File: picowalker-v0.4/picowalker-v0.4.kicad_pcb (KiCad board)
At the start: 4 copper layers, 47.4 x 50.5 mm, 86 parts, among them IC1 RT6150B-33GQW, J1 12402012E212A, J2 BAT, J3 SWD, J4 UART, SW1 ~{BOOT}, SW2 RUN, SW3 BUT_M, SW4 BUT_R, SW5 BUT_L, U1 RP2350A-QFN60, U2 W25Q128JVP, U3 BMA400, U4 M95512DxMC, U5 TFBS4711, U6 BQ25628ERYKR, U7 DO0180FMST0x, Y1 ABM8-272-T3, Y2 SIT1533AI-H4-DCC-32.768E

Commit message: v0.4: good start on routing
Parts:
- removed C15: 0.1u, Capacitor_SMD:C_0402_1005Metric
- added R23: 5.1k, Resistor_SMD:R_0402_1005Metric, F.Cu at (160.1, 108.2)
- added R24: 5.1k, Resistor_SMD:R_0402_1005Metric, F.Cu at (161.6, 108.3)
- added TP6: GP16, picowalker:TestPoint_Pad_D1.0mm_Nosilk, F.Cu at (134.2, 89.7)
- added TP7: GP17, picowalker:TestPoint_Pad_D1.0mm_Nosilk, F.Cu at (131.9, 90.5)
- added U8: DT1240-04LP-7, picowalker:U-DFN2510-10, B.Cu at (148.8, 116.3)
- L2: footprint Inductor_SMD:L_0402_1005Metric -> Inductor_SMD:L_0603_1608Metric
- R2, SW2: moved to B.Cu
- TP1: value MCU_1V1 -> ~{PG}; footprint TestPoint:TestPoint_Pad_1.0x1.0mm -> picowalker:TestPoint_Pad_D1.0mm_Nosilk; moved to F.Cu
- TP2: footprint TestPoint:TestPoint_Pad_1.0x1.0mm -> picowalker:TestPoint_Pad_D1.0mm_Nosilk; moved to F.Cu
- U4: footprint picowalker:XDFN8 -> picowalker:UFDFPN8
- moved R19 29.0 mm to (172.2, 103.4), turned to 180 degrees
- moved TP1 28.2 mm to (173.6, 105.5), turned to 0 degrees
- moved SW2 26.5 mm to (167.1, 85.4), turned to 180 degrees
- moved R2 19.1 mm to (163.1, 84.4), turned to 0 degrees
- moved R9 17.3 mm to (155.4, 113.2), turned to 180 degrees
- moved R12 16.5 mm to (155.4, 112.2)
- moved C17 15.9 mm to (155.4, 111.2)
- moved R15 9.92 mm to (128.9, 102.0), turned to -90 degrees
- moved R7 9.73 mm to (152.6, 115.8), turned to 0 degrees
- moved R10 9.62 mm to (144.1, 113.1), turned to 180 degrees
- moved R13 9.62 mm to (144.1, 112.1)
- moved C18 7.76 mm to (144.1, 111.1)
- moved C22 7.14 mm to (128.9, 100.1), turned to -90 degrees
- moved R20 6.38 mm to (145.0, 106.3)
- moved C20 6.31 mm to (134.1, 95.3), turned to 90 degrees
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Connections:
- net /accel/INT renamed /ACCEL_INT
- net /accel/~{CS} renamed /~{ACCEL_CS}
- net /eeprom/~{CS} renamed /~{EEPROM_CS}
- net /mcu/SOUND_PWM renamed /SOUND
- net /mcu/~{BAT_INT} renamed /~{BAT_INT}
- net /mcu/~{CE} renamed /~{BAT_CE}
- net /screen/SCL renamed /screen/TP_I2C.SCL
- net /screen/SDA renamed /screen/TP_I2C.SDA
- net Net-(U6-PMID) renamed /power/PMID
- net Net-(U6-SW) renamed /power/SW
- net Net-(U6-~{QON}) renamed /power/~{QON}
- J3 pad 1: /connectors/SWCLK -> /connectors/SWD.SWCLK
- J3 pad 3: /connectors/SWDIO -> /connectors/SWD.SWDIO
- J4 pad 1: /connectors/RX -> /connectors/DBG_UART.RX
- J4 pad 3: /connectors/TX -> /connectors/DBG_UART.TX
- R16 pad 1: /eeprom/SCK -> /accel/SPI.SCK
- TP1 pad 1: +1.1V -> /power/~{PG}
- U1 pad 10: /mcu/~{RST} -> /mcu/SCREEN_DATA.SCK
- U1 pad 12: /mcu/SCK -> /mcu/SCREEN_DATA.SD3
- U1 pad 13: /mcu/SD3 -> /mcu/SCREEN_DATA.SD2
- U1 pad 14: /mcu/SD2 -> /mcu/SCREEN_DATA.SD1
- U1 pad 15: /mcu/SD1 -> /mcu/SCREEN_DATA.SD0
- U1 pad 16: /mcu/SD0 -> /mcu/SCREEN_AUX.~{RST}
- U1 pad 17: /mcu/TX -> /IRDA_SD
- U1 pad 18: /mcu/RX -> /irda/IRDA.RX
- U1 pad 19: /irda/SD -> /irda/IRDA.TX
- U1 pad 2: /mcu/SDA -> /mcu/I2C.SDA
- U1 pad 24: /mcu/SWCLK -> /connectors/SWD.SWCLK
- U1 pad 25: /mcu/SWDIO -> /connectors/SWD.SWDIO
- U1 pad 27: /mcu/M -> /mcu/GP16
- U1 pad 28: /mcu/L -> /mcu/GP17
- U1 pad 29: /mcu/SCK -> /accel/SPI.SCK
- U1 pad 3: /mcu/SCL -> /mcu/I2C.SCL
- U1 pad 31: /mcu/MOSI -> /accel/SPI.MOSI
- U1 pad 32: /mcu/MISO -> /accel/SPI.MISO
- U1 pad 37: unconnected-(U1-GPIO25-Pad37) -> /buttons/BUT.L
- U1 pad 40: /mcu/R -> /buttons/BUT.M
- U1 pad 41: unconnected-(U1-GPIO27_ADC1-Pad41) -> /buttons/BUT.R
- U1 pad 42: /mcu/TX -> /connectors/DBG_UART.TX
- U1 pad 43: /mcu/RX -> /connectors/DBG_UART.RX
- U1 pad 55: /mcu/SD3 -> /flash/QSPI.SD3
- U1 pad 56: /mcu/SCK -> /flash/QSPI.SCK
- U1 pad 57: /mcu/SD0 -> /flash/QSPI.SD0
- U1 pad 58: /mcu/SD2 -> /flash/QSPI.SD2
- U1 pad 59: /mcu/SD1 -> /flash/QSPI.SD1
- U1 pad 8: /mcu/~{SCREEN_CS} -> /mcu/SCREEN_AUX.PWR_EN
- U1 pad 9: /mcu/PWR_EN -> /~{SCREEN_CS}
- U2 pad 2: /flash/SD1 -> /flash/QSPI.SD1
- U2 pad 3: /flash/SD2 -> /flash/QSPI.SD2
- U2 pad 5: /flash/SD0 -> /flash/QSPI.SD0
- U2 pad 6: /flash/SCK -> /flash/QSPI.SCK
- U2 pad 7: /flash/SD3 -> /flash/QSPI.SD3
- U3 pad 1: /accel/MISO -> /accel/SPI.MISO
- U3 pad 12: /accel/SCK -> /accel/SPI.SCK
- U3 pad 2: /accel/MOSI -> /accel/SPI.MOSI
- U4 pad 2: /eeprom/MISO -> /accel/SPI.MISO
- U4 pad 5: /eeprom/MOSI -> /accel/SPI.MOSI
- U4 pad 6: /eeprom/SCK -> /accel/SPI.SCK
- U5 pad 2: /irda/TX -> /irda/IRDA.TX
- U5 pad 3: /irda/RX -> /irda/IRDA.RX
- U5 pad 4: /irda/SD -> /IRDA_SD
- U6 pad 12: /power/SDA -> /mcu/I2C.SDA
- U6 pad 13: /power/SCL -> /mcu/I2C.SCL
- U7 pad 1: /screen/~{RST} -> /mcu/SCREEN_AUX.~{RST}
- U7 pad 11: /mcu/~{SCREEN_CS} -> /~{SCREEN_CS}
- U7 pad 13: /screen/SD2 -> /mcu/SCREEN_DATA.SD2
- U7 pad 15: /screen/SD3 -> /mcu/SCREEN_DATA.SD3
- U7 pad 16: unconnected-(U7-TP_VCC-Pad16) -> /screen/TP_VCC
- U7 pad 2: unconnected-(U7-TE-Pad2) -> /screen/TE
- U7 pad 22: /screen/PWR_EN -> /mcu/SCREEN_AUX.PWR_EN
- U7 pad 5: /screen/SD0 -> /mcu/SCREEN_DATA.SD0
- U7 pad 7: /screen/SD1 -> /mcu/SCREEN_DATA.SD1
- U7 pad 9: /screen/SCK -> /mcu/SCREEN_DATA.SCK
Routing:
- net +3.3V: track 8.30 -> 43.3 mm, vias 0 -> 8
- net /buttons/BUT.M: track 0.00 -> 33.8 mm
- net /mcu/RUN: track 0.00 -> 30.2 mm, vias 0 -> 1
- net /buttons/BUT.L: track 0.00 -> 29.3 mm
- net GND: track 10.2 -> 36.3 mm, vias 2 -> 16
- net /accel/SPI.SCK: track 0.00 -> 26.0 mm
- net /~{BAT_CE}: track 0.00 -> 25.3 mm, vias 0 -> 2
- net /SOUND: track 0.00 -> 24.1 mm, vias 0 -> 1
- net /accel/SPI.MISO: track 0.00 -> 24.0 mm, vias 0 -> 3
- net /mcu/SCREEN_AUX.~{RST}: track 0.00 -> 23.9 mm, vias 0 -> 1
- net +1.1V: track 2.06 -> 25.9 mm, vias 2 -> 9
- net /~{BAT_INT}: track 0.00 -> 23.4 mm
- net /mcu/I2C.SCL: track 0.00 -> 23.2 mm, vias 0 -> 2
- net /mcu/I2C.SDA: track 0.00 -> 21.8 mm, vias 0 -> 2
- net /~{SCREEN_CS}: track 0.00 -> 21.5 mm, vias 0 -> 1
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- added copper zone on F.Cu, net +3.3V
- added copper zone on F.Cu, net /connectors/BAT+
- added copper zone on In2.Cu, net /connectors/BAT+
- added copper zone on F.Cu, net /power/PMID
- added copper zone on F.Cu, net /power/SW
- added copper zone on In2.Cu, net /power/SW
- added copper zone on F.Cu, net VBUS
- added copper zone on In2.Cu, net VBUS
- added copper zone on F.Cu, net VSYS
- added copper zone on In2.Cu, net VSYS
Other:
- board text added: "${TITLE} ${REVISION}"
- board text added: "KEEP VIAS OUT OF INNER CIRCLE TO PREVENT SHORTS IF SCREW IS TOO LONG"

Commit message: v0.4: running DRC checks
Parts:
- TH1: moved to B.Cu
- U8: footprint picowalker:U-DFN2510-10 -> picowalker:U-DFN2510-10_oneside
- moved R22 16.8 mm to (156.7, 111.4), turned to -90 degrees
- moved R20 13.8 mm to (158.6, 108.5), turned to 90 degrees
- moved D1 12.4 mm to (155.8, 122.2), turned to 90 degrees
- moved TH1 5.51 mm to (150.4, 108.8), turned to 90 degrees
- moved R9 4.11 mm to (155.7, 109.1), turned to -90 degrees
- moved R24 4.09 mm to (160.1, 104.5), turned to -90 degrees
- moved R23 4.03 mm to (161.7, 104.5), turned to -90 degrees
- moved R12 3.18 mm to (154.7, 109.1), turned to 90 degrees
- moved C17 2.70 mm to (153.7, 109.1), turned to 90 degrees
- moved U8 1.88 mm to (147.1, 115.5)
- moved J4 0.28 mm to (132.4, 106.5)
- moved TP1 0.14 mm to (173.5, 105.5)
- moved C36 0.10 mm to (163.8, 98.7), turned to 180 degrees
- turned SW3 to 0 degrees
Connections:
- net /screen/TE renamed /TE
- net /screen/TP_INT renamed /TP_INT
- net /screen/TP_RESET renamed /TP_RESET
- U6 pad 10: /power/STAT -> /power/~{STAT}
- U8 pad 4: unconnected-(U8-IO3-Pad4) -> VBUS
- U8 pad 5: VBUS -> unconnected-(U8-IO4-Pad5)
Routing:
- net GND: track 36.3 -> 65.3 mm, vias 16 -> 91
- net /power/TS: track 3.31 -> 31.5 mm, vias 1 -> 2
- net /power/~{STAT}: track 0.00 -> 26.4 mm, vias 0 -> 2
- net /buttons/BUT.R: track 8.02 -> 32.9 mm, vias 1 -> 2
- net +3.3V: track 43.3 -> 61.9 mm, vias 8 -> 23
- net /connectors/USB.DN: track 3.65 -> 18.9 mm, vias 0 -> 1
- net /connectors/USB.DP: track 5.32 -> 19.7 mm, vias 0 -> 1
- net /buttons/BUT_M_1: track 1.00 -> 14.5 mm
- net /buttons/BUT_R_1: track 0.00 -> 11.0 mm
- net Net-(D1-A): track 0.00 -> 10.2 mm
- net /TP_INT: track 6.89 -> 0.00 mm, vias 1 -> 0
- net /screen/TP_VCC: track 6.85 -> 0.00 mm, vias 1 -> 0
- net /TP_RESET: track 6.69 -> 0.00 mm, vias 1 -> 0
- net +1.1V: track 25.9 -> 32.3 mm
- net VSYS: track 5.16 -> 11.4 mm, vias 14 -> 15
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- added copper zone on In2.Cu, net +3.3V
- added copper zone on B.Cu, net GND
- added copper zone on In1.Cu, net GND
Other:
- outline, holes or cut-outs redrawn

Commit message: v0.4: drc mostly done, need to fiddle with TH1
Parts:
- added REF**: Tab, PCM_kikit:Tab, F.Cu at (173.7, 89.3)
- added REF**: Tab, PCM_kikit:Tab, F.Cu at (150.0, 74.2)
- added REF**: Tab, PCM_kikit:Tab, F.Cu at (127.3, 99.8)
- added REF**: Tab, PCM_kikit:Tab, F.Cu at (150.0, 125.2)
- added REF**: Tab, PCM_kikit:Tab, F.Cu at (175.2, 104.0)
- added TP3: 32k, picowalker:TestPoint_Pad_D1.0mm_Nosilk, F.Cu at (139.3, 94.1)
- added TP4: GND, picowalker:TestPoint_Pad_D1.0mm_Nosilk, F.Cu at (133.9, 93.3)
- C20, C21: value 4.7u -> 0.1u
- J3, J4: footprint Connector_JST:JST_SH_SM03B-SRSS-TB_1x03-1MP_P1.00mm_Horizontal -> picowalker:JST_SH_SM03B-SRSS-TB_1x03-1MP_P1.00mm_Horizontal_wider
- R2: moved to F.Cu
- U1: footprint Package_DFN_QFN:QFN-60-1EP_7x7mm_P0.4mm_EP3.4x3.4mm_ThermalVias -> picowalker:QFN-60-1EP_7x7mm_P0.4mm_EP3.4x3.4mm_ThermalVias
- moved R2 21.8 mm to (141.9, 89.5)
- moved C18 4.60 mm to (145.1, 106.6)
- moved R10 4.60 mm to (145.1, 108.6)
- moved R13 4.60 mm to (145.1, 107.6)
- moved BZ1 2.20 mm to (156.4, 113.9)
- moved C19 1.91 mm to (140.8, 106.2)
- moved R11 1.91 mm to (140.8, 108.2)
- moved R14 1.91 mm to (140.8, 107.2)
- moved SW2 0.81 mm to (167.0, 86.2)
- moved SW1 0.54 mm to (167.0, 89.7)
- moved Y2 0.45 mm to (136.8, 94.1)
- moved SW3 0.42 mm to (150.0, 118.4)
- moved TH1 0.40 mm to (150.0, 108.8)
- moved SW4 0.24 mm to (162.0, 116.7)
- moved SW5 0.18 mm to (138.0, 116.7)
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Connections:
- R2 pad 1: GND -> /mcu/SW_RUN_P
- R2 pad 2: Net-(SW2-A) -> /mcu/RUN
- SW2 pad 1: Net-(SW2-A) -> GND
- SW2 pad 2: /mcu/RUN -> /mcu/SW_RUN_P
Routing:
- net /mcu/SW_RUN_P: track 0.00 -> 30.9 mm, vias 0 -> 1
- net /mcu/RUN: track 33.8 -> 5.29 mm, vias 1 -> 0
- net Net-(SW2-A): track 5.19 -> 0.00 mm
- net /buttons/BUT_M_1: track 14.5 -> 19.3 mm
- net /buttons/BUT_L_1: track 7.07 -> 9.15 mm
- net /buttons/BUT.L: track 29.3 -> 30.7 mm
- net /mcu/RTC_CLK: track 5.78 -> 6.63 mm
- net /buttons/BUT.M: track 33.8 -> 33.2 mm
- net GND: track 65.3 -> 65.7 mm, vias 91 -> 95
- net +3.3V: track 61.9 -> 62.2 mm, vias 23 -> 25
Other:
- board text added: "+"
- board text added: "-"
- board text added: "32k"
- board text added: "3V3"
- board text added: "BOOT"
- board text added: "Battery"
- board text added: "Battery (502530)"
- board text added: "GND"
- board text added: "GP16"
- board text added: "GP17"
- board text added: "RUN"
- board text added: "RX"
- board text added: "SWCLK"
- board text added: "SWDIO"
- board text added: "Speaker"
- board text added: "TX"

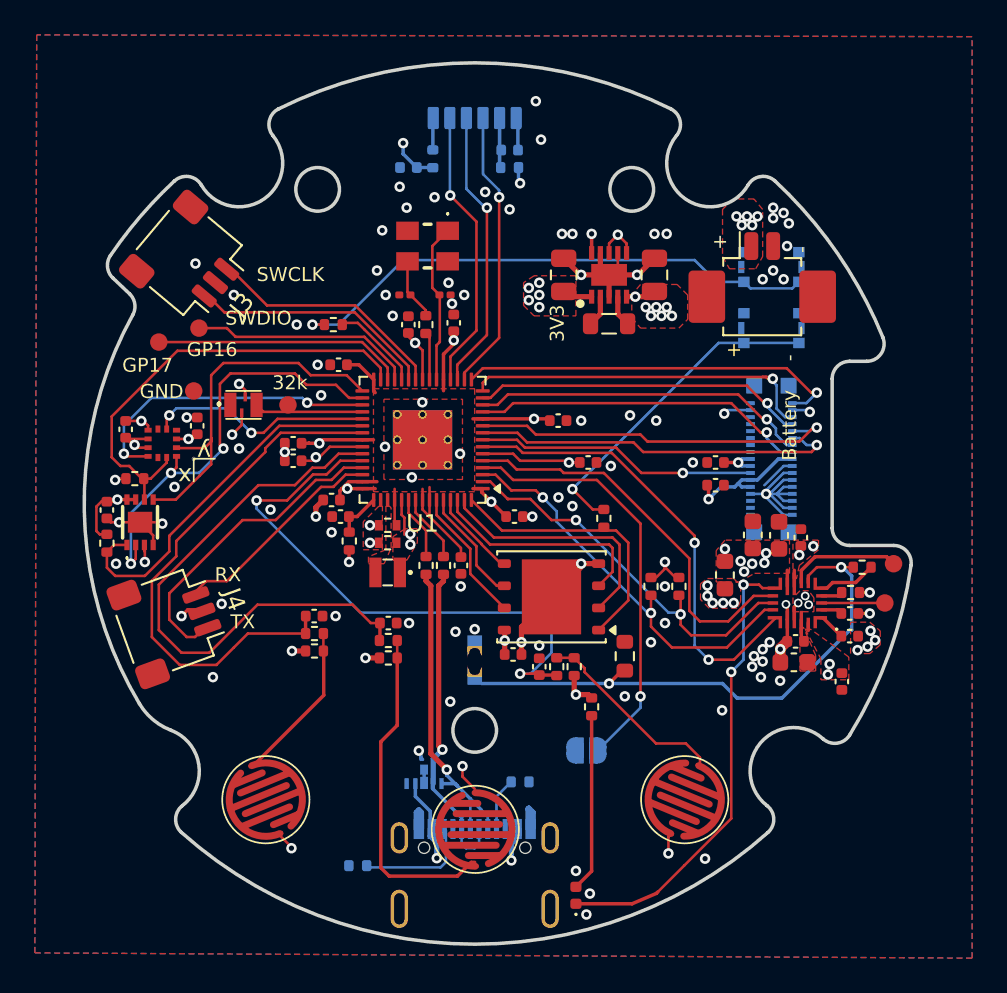
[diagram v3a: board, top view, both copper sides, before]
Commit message: v0.4: update readme and add renders
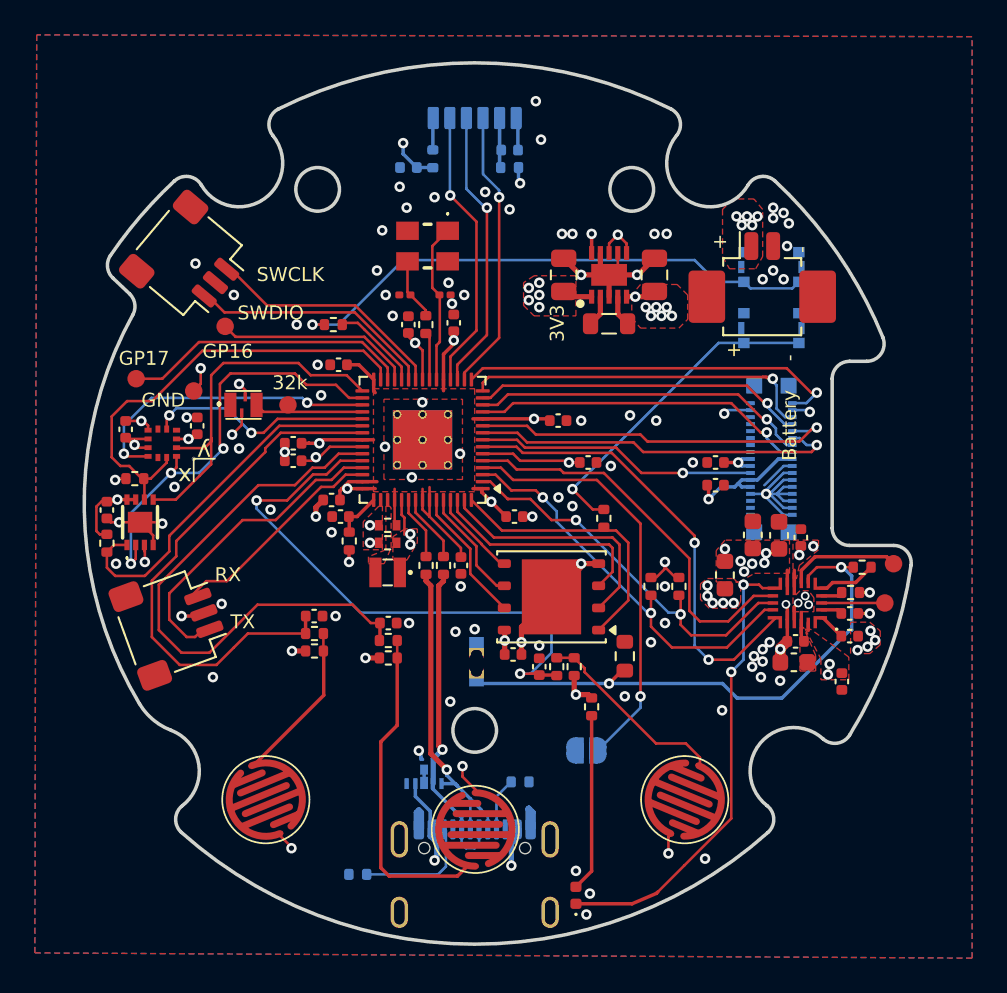
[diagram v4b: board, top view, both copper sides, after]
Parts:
- J1: footprint picowalker:USBC -> Connector_USB:USB_C_Receptacle_GCT_USB4105-xx-A_16P_TopMnt_Horizontal
- moved J1 3.70 mm to (150.0, 122.1)
- moved TP7 2.47 mm to (130.6, 92.6)
- moved TP6 1.50 mm to (135.7, 89.6)
- moved R8 0.50 mm to (143.3, 121.0)
- moved J4 0.15 mm to (132.6, 106.7)
- moved TH1 0.14 mm to (150.1, 108.9)
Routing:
- net /mcu/GP17: track 14.5 -> 16.6 mm
- net GND: track 65.7 -> 67.5 mm, vias 95 -> 96
- net /mcu/GP16: track 12.9 -> 11.4 mm
